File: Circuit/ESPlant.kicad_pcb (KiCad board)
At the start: 2 copper layers, 10.3 x 5.9 mm, 64 parts, among them P1 SOIL, P101 CONN_DIGITAL, P102 CONN_ANALOG, P103 CONN_SERIAL, P104 CONN_I2C, P105 SOLAR, P106 USB_5PIN_SHELL, P109 CONN_PWR, P110 CONN_01X05, P111 UV, P112 TEMP, P113 NEOPIXEL, P114 PIR, Q101 FDN340P, Q201 FDN340P, Q202 FDN340P, Q203 FDN340P, SW101 RESET, SW102 PRGM, SW103 RESET, U101 STM32F042F, U103 ESP-12E, U201 CN3063, U202 MCP6002, U301 BME280, U302 ADXL345

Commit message: Better routing pass
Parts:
- moved R302 30.0 mm to (207.6, 106.5)
- moved R301 24.0 mm to (210.1, 108.3)
- moved P106 8.90 mm to (146.1, 65.9)
- moved P112 6.90 mm to (235.5, 83.6)
- moved P113 6.90 mm to (235.5, 114.1)
- moved P111 6.90 mm to (145.5, 121.1)
- moved P105 6.90 mm to (145.5, 74.1)
- moved P1 6.90 mm to (145.5, 105.6)
- moved P114 6.90 mm to (235.5, 99.1)
- moved C301 6.58 mm to (227.5, 126.4)
- moved U301 6.58 mm to (231.5, 127.0)
- moved SJ101 1.32 mm to (203.0, 122.5), turned to 270 degrees
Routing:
- net /VCC_SENS: track 180.9 -> 228.4 mm, vias 2 -> 0
- net /I2C Sensors/I2C_SDA: track 106.1 -> 121.2 mm, vias 2 -> 5
- net GND: track 90.0 -> 104.4 mm, vias 21 -> 23
- net /I2C Sensors/I2C_SCL: track 111.2 -> 122.3 mm, vias 2 -> 5
- net /GPIO12: track 57.3 -> 67.4 mm
- net /USB_D-: track 54.4 -> 63.4 mm
- net /USB_D+: track 52.9 -> 61.9 mm
- net /Power/USB_IN: track 23.0 -> 31.9 mm
- net +3V3: track 198.4 -> 206.9 mm, vias 8 -> 9
- net /SOIL_1: track 31.4 -> 39.5 mm, vias 2 -> 3
- net /GPIO15: track 75.6 -> 83.1 mm, vias 1 -> 3
- net /ADC0: track 31.2 -> 38.2 mm, vias 2 -> 3
- net /SOIL_2: track 29.0 -> 35.9 mm, vias 2 -> 3
- net /GPIO13: track 33.2 -> 40.1 mm
- net /Power/SOLAR_IN: track 6.33 -> 12.8 mm
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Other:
- board size 10.3 x 5.9 mm -> 97 x 74 mm

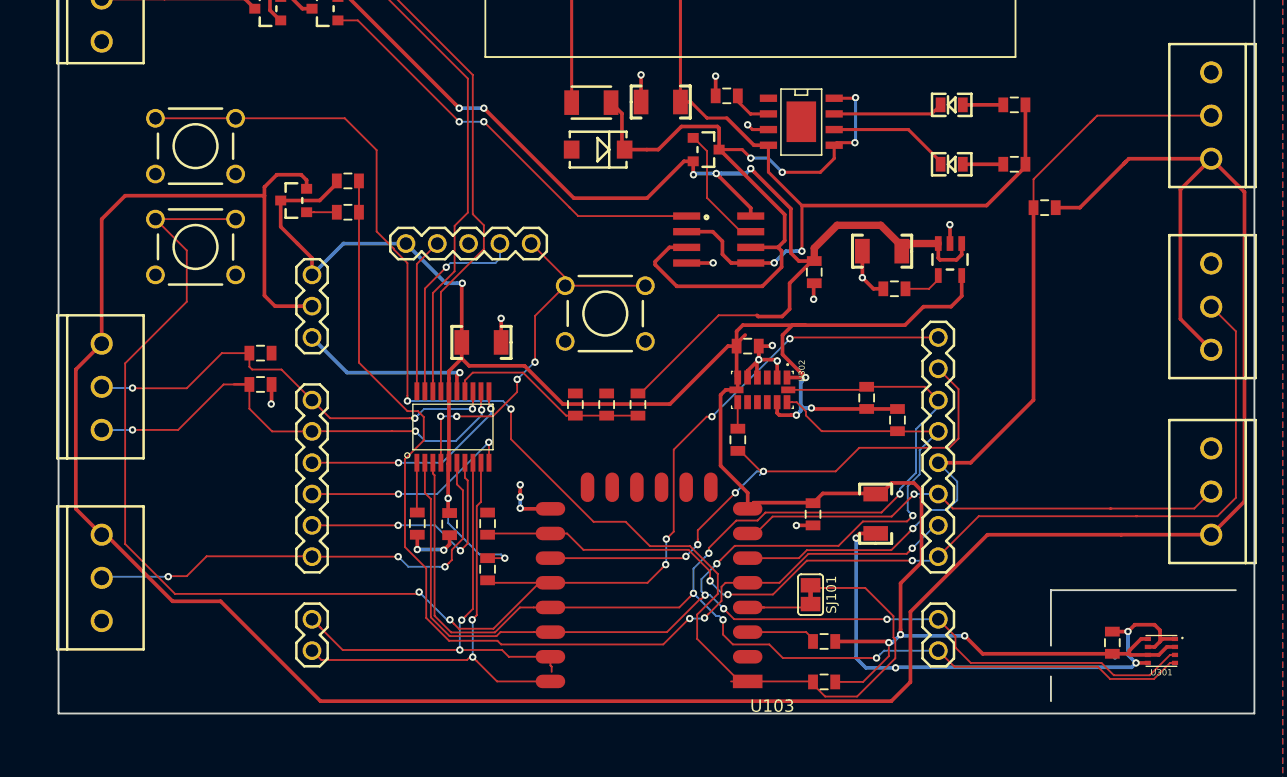
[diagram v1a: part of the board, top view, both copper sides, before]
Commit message: Shrink back ground plane slots some more
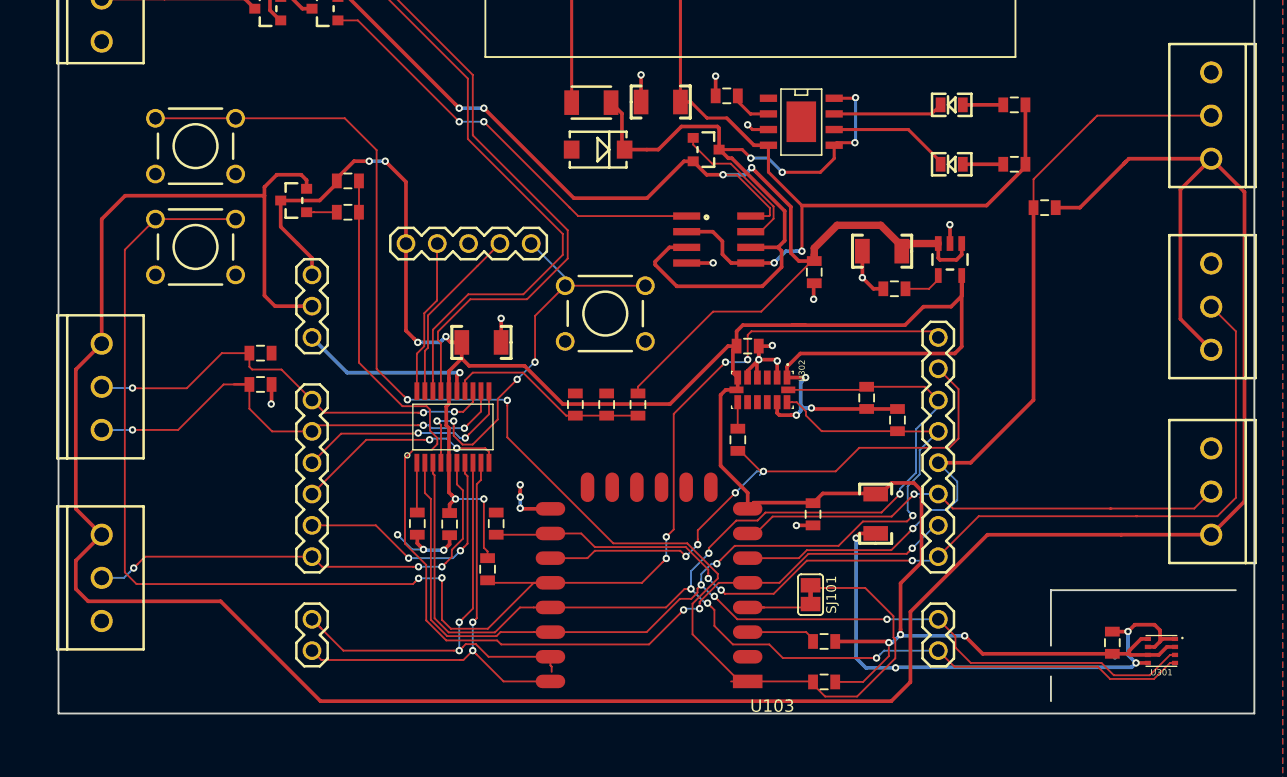
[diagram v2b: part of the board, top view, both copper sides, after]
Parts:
- moved R109 0.70 mm to (177.5, 116.7)
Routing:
- net +3V3: track 206.9 -> 226.0 mm, vias 9 -> 12
- net /USB_D+: track 61.9 -> 70.9 mm
- net /USB_D-: track 63.4 -> 71.9 mm
- net /VCC_SENS: track 228.4 -> 233.9 mm
- net /GPIO0: track 125.0 -> 129.5 mm
- net /STM_~RESET: track 32.1 -> 35.7 mm
- net /Power/GBAT: track 10.0 -> 12.4 mm
- net GND: track 104.4 -> 106.7 mm, vias 23 -> 24
- net /GPIO14: track 86.6 -> 88.8 mm
- net /STM_SWDIO: track 16.6 -> 14.5 mm, vias 1 -> 0
- net /GPIO15: track 83.1 -> 82.1 mm
- net /Power/VOUT: track 97.6 -> 96.9 mm, vias 5 -> 4
- net /SOIL_2: track 35.9 -> 35.2 mm
- net /SOIL_1: track 39.5 -> 38.9 mm
- net /STM_TXD: track 38.7 -> 39.3 mm
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
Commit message: Routing finished?
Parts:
- added 1pin: VAL**, Connect:1pin, F.Cu at (155.5, 64.6)
- added 1pin: VAL**, Connect:1pin, F.Cu at (145.5, 134.6)
- added 1pin: VAL**, Connect:1pin, F.Cu at (235.5, 134.6)
- added 1pin: VAL**, Connect:1pin, F.Cu at (235.5, 64.6)
- moved Q202 47.9 mm to (208.2, 92.6)
- moved F101 44.9 mm to (228.0, 68.9)
- moved D101 44.2 mm to (227.9, 73.0)
- moved Q203 14.1 mm to (208.5, 88.3), turned to 0 degrees
- moved C202 13.2 mm to (191.4, 90.7), turned to 90 degrees
- moved Q201 12.4 mm to (169.6, 68.6), turned to 0 degrees
- moved C203 9.75 mm to (218.5, 95.6), turned to 90 degrees
- moved C106 4.94 mm to (204.9, 112.3), turned to 0 degrees
- moved R102 4.80 mm to (159.4, 110.1), turned to 270 degrees
- moved C301 4.70 mm to (232.2, 126.5)
- moved U301 4.70 mm to (236.2, 127.1)
- moved R103 1.71 mm to (159.4, 101.5), turned to 90 degrees
- moved P105 1.50 mm to (145.5, 75.6)
- moved P106 1.44 mm to (146.1, 67.3)
- moved U202 1.05 mm to (196.4, 93.1), turned to 0 degrees
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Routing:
- net GND: track 106.7 -> 150.8 mm, vias 24 -> 61
- net /Power/VOUT: track 96.9 -> 62.4 mm, vias 4 -> 0
- net /Power/SOLAR_IN: track 12.8 -> 34.6 mm, vias 0 -> 2
- net /Power/GIN: track 34.9 -> 17.8 mm, vias 2 -> 0
- net /USB_D+: track 70.9 -> 80.5 mm
- net /USB_D-: track 71.9 -> 80.6 mm
- net +3V3: track 226.0 -> 234.2 mm
- net /Power/GBAT: track 12.4 -> 19.5 mm, vias 0 -> 2
- net /I2C Sensors/I2C_SCL: track 122.5 -> 128.5 mm
- net /SOIL_1: track 38.9 -> 33.4 mm
- net /I2C Sensors/I2C_SDA: track 121.5 -> 125.8 mm
- net /SOIL_2: track 35.2 -> 39.1 mm
- net /BAT+: track 14.5 -> 17.9 mm
- net /Power/USB_IN: track 31.9 -> 29.3 mm, vias 2 -> 0
- net /STM_SWDIO: track 14.5 -> 16.6 mm
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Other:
- board size 97 x 74 mm -> 97 x 77.5 mm
- board text added: "(GPIO0)"
- board text added: "+"
- board text added: "+3.3V"
- board text added: "+VSen"
- board text added: "-"
- board text added: "/4"
- board text added: "/5"
- board text added: "ADC0"
- board text added: "ADC1"
- board text added: "ADC2"
- board text added: "ADC3"
- board text added: "ADC4"
- board text added: "ADC5"
- board text added: "Designed for LCA2016 Open Hardware MiniConf by Angus Gratton & John Spencer http://github.com/mage0r/ESPlant TAPR Open Hardware License"
- board text added: "ESP FLASH"
- board text added: "ESP RESET"
- board text added: "ESPlant"
- board text added: "GND"
- board text added: "GPIO0"
- board text added: "GPIO12"
- board text added: "GPIO13"
- board text added: "GPIO14"
- board text added: "GPIO15"
- board text added: "GPIO2"
- board text added: "MAX 7V/1A"
- board text added: "PIR SENSOR"
- board text added: "RX (GPIO3)"
- board text added: "SCL"
- board text added: "SDA"
- board text added: "SOIL MOISTURE"
- board text added: "SOLAR PANEL"
- board text added: "STM DEBUG"
- board text added: "STM RESET"
- board text added: "SWCLK"
- board text added: "SWDIO"
- board text added: "TEMP SENSOR"
- board text added: "TX (GPIO1)"
- board text added: "UV SENSOR"
- board text added: "V1.0B"
- board text added: "WS2812B LEDS"
- board text added: "~RST"

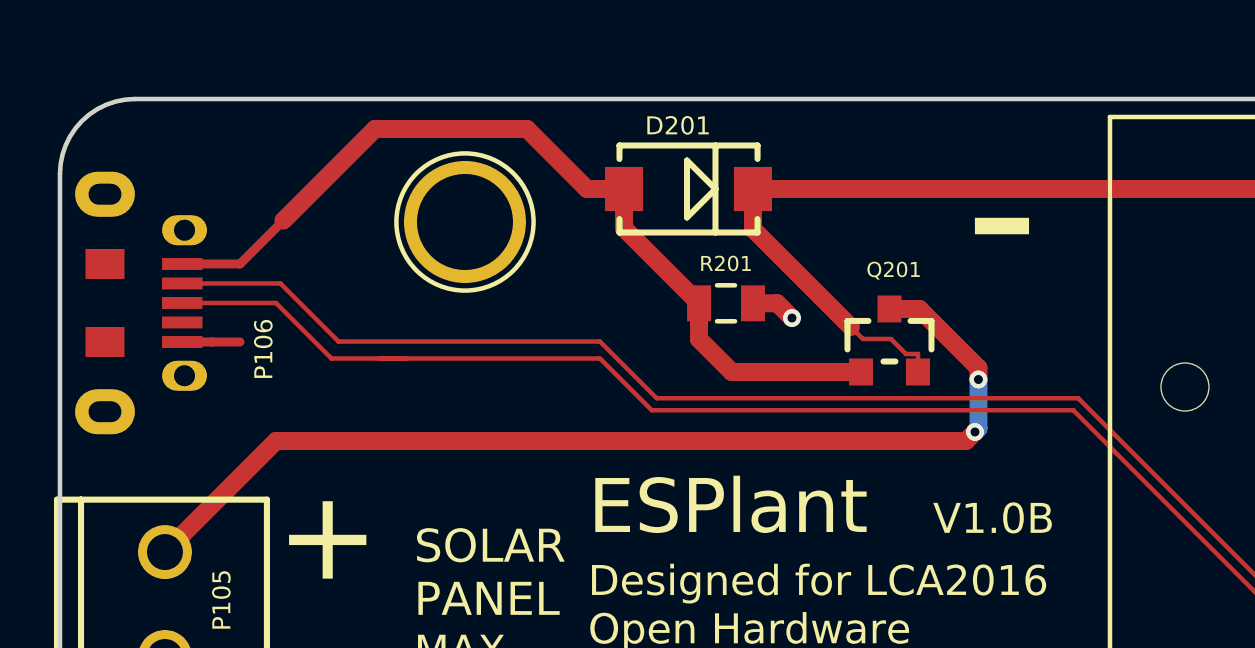
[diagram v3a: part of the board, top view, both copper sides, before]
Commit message: Add crowbar diode for solar panel polarity protection
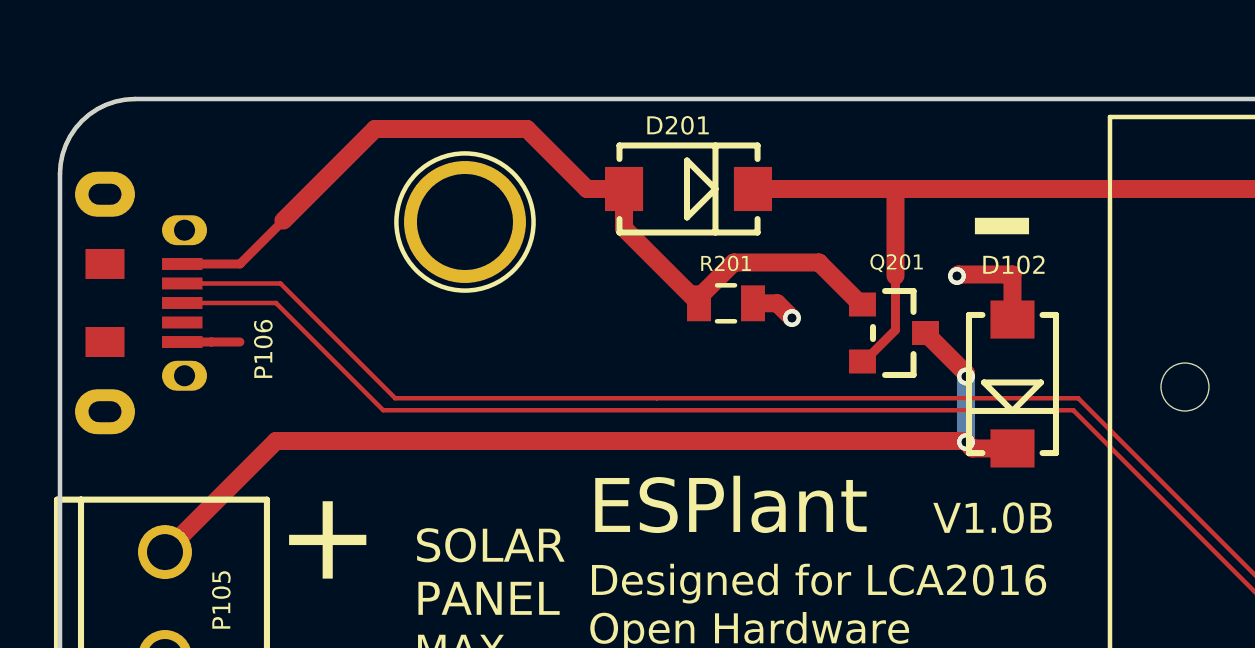
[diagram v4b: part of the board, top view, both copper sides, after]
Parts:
- added D102: SS14, FT:DIODE_SMA, F.Cu at (173.8, 70.0)
- moved Q201 0.32 mm to (169.8, 68.3), turned to 270 degrees
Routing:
- net GND: track 150.8 -> 154.2 mm, vias 61 -> 62
- net /Power/VIN: track 119.5 -> 116.6 mm
- net /USB_D+: track 80.5 -> 79.7 mm
- net /Power/SOLAR_IN: track 34.6 -> 34.1 mm

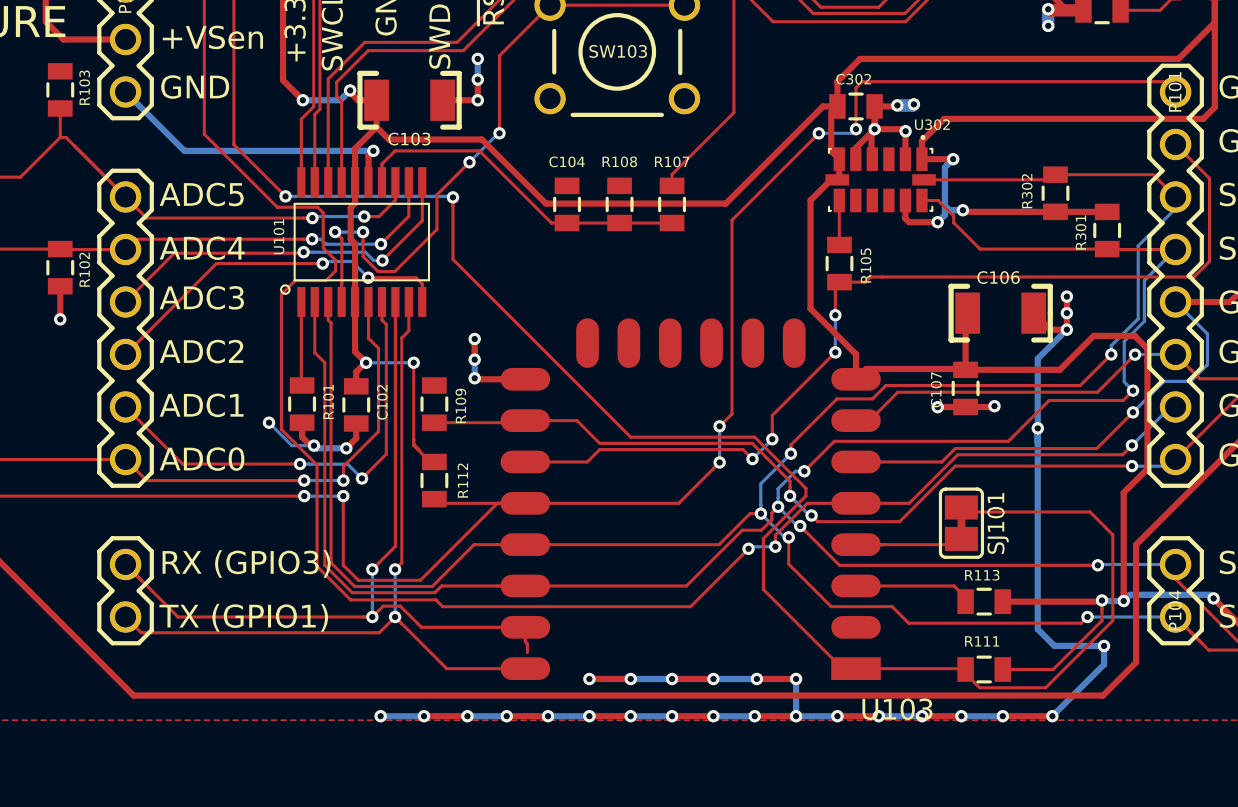
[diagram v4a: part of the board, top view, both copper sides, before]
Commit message: Revise schematic for V1.1 based on V1.0 evaluation:
* Swap SDA, SCL on ESP (5,4 to 4,5) to match Arduino default
* Q101 source, drain were swapped
* BME280 change i2c address config  0x76 -> 0x77 (match Adafruit library)
* ADXL345 change i2c address from 0x1d -> 0x53 (match Adafruit library)
* Specify colours for "charging", "done" LEDs in component values
* R202, R203 LED series resistors changed to 1K
* Add GPIO2 pullup to strapping resistors, required for reliable reset
* Add autoreset: connect ESP_RESET to PA7 on STM32, GPIO0 to PB8. Remove
  "ADC5" pin from design.
* Add 1K series resistor between GPIO16 and RESET (replacing solder
  jumper). Otherwise pulling reset line draws >50mA!!
* Add 1K series resistor from GPIO0 to GPIO0 reset button & STM32
  GPIO. This is because GPIO0 defaults to clock output on reset,
  driving a square wave.
* Change 220uF 1210 bulk capacitor value to 100uF, reflecting part
  availability and reliability shown in testing.
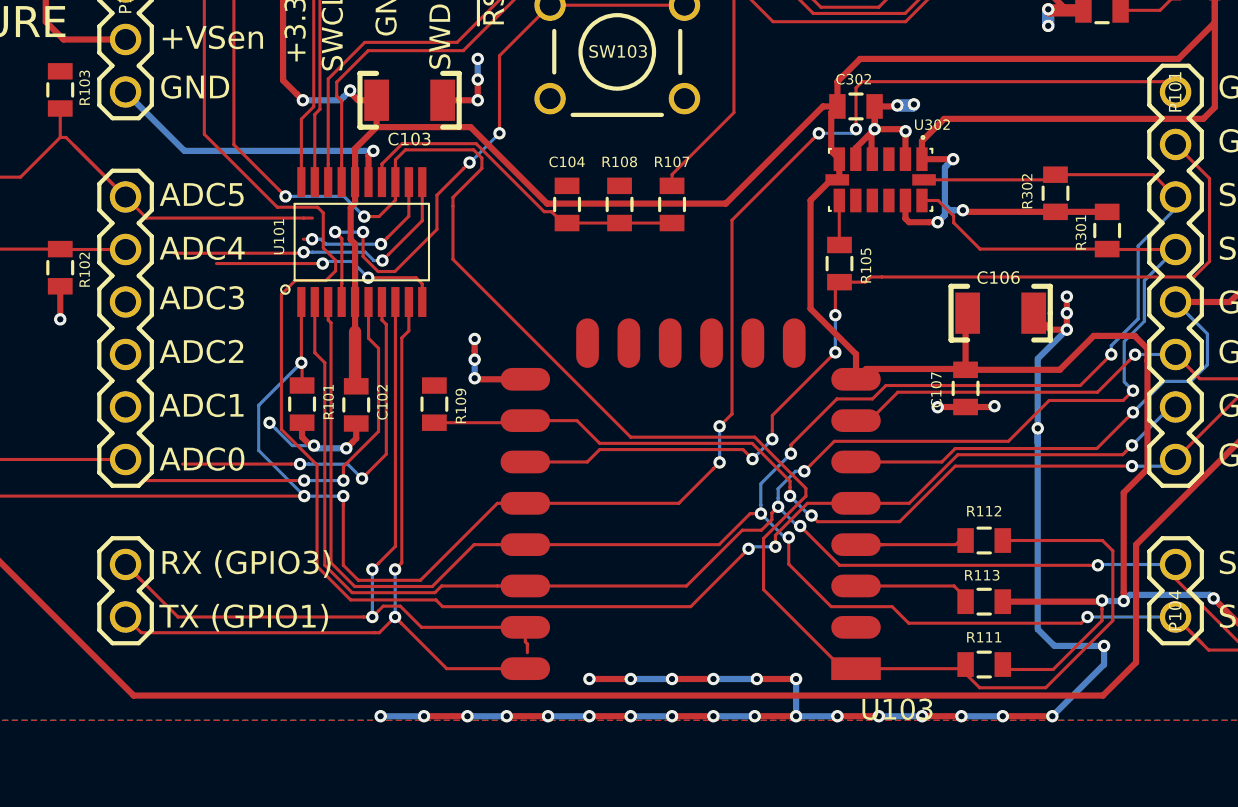
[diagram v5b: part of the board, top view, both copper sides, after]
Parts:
- removed SJ101: SJ, FT:SJ_SHORTED
- MH101, MH102, MH103, MH104: renamed from 1pin; value VAL** -> TEST_1P
- moved R112 26.8 mm to (204.1, 123.3), turned to 180 degrees
- moved R111 0.24 mm to (204.1, 129.3), turned to 180 degrees
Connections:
- P102 pad 4: /ADC3 -> (no net)
- R101 pad 1: /STM_BOOT -> /GPIO0
- R111 pad 1: /ESP_~RESET -> +3V3
- R111 pad 2: +3V3 -> /ESP_~RESET
- R112 pad 1: /GPIO0 -> /ESP_~RESET
- R112 pad 2: +3V3 -> /GPIO16
- U101 pad 1: /STM_BOOT -> /GPIO0
- U101 pad 11: /ADC3 -> /SOIL_1
- U101 pad 12: /SOIL_1 -> /SOIL_2
- U101 pad 13: /SOIL_2 -> /ESP_~RESET
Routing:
- net /ADC3: track 18.2 -> 0.00 mm, vias 2 -> 0
- net +3V3: track 234.2 -> 225.6 mm, vias 12 -> 10
- net /GPIO0: track 128.6 -> 136.4 mm, vias 6 -> 7
- net /ADC2: track 17.6 -> 11.3 mm
- net /ESP_~RESET: track 110.5 -> 114.6 mm
- net /STM_BOOT: track 4.05 -> 0.00 mm
- net /ADC1: track 22.0 -> 18.1 mm
- net /SOIL_2: track 39.1 -> 41.3 mm
- net /ADC0: track 38.3 -> 36.8 mm
- net /SOIL_1: track 33.4 -> 32.7 mm
